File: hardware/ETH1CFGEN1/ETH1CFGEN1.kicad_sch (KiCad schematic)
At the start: 0 parts

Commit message: Development
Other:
- sheet ADC ports: added ADC_CLK, ADC_CONV, ADC_DATA, MEAS_AMPL, MEAS_BUF, MEAS_MOD_DAC, MEAS_OUT, MSEL[0..2]; removed none
- sheet Connector ports: added MAIN_OUTPUT; removed SIGNAL
- sheet DAC ports: added DAC_DIN, DAC_SCLK, DAC_nCLR, DAC_nLDAC, DAC_nSYNC; removed none
- sheet MCU ports: added I2C2_SCL, I2C2_SDA, SPI2_CLK, SPI2_CS, SPI2_MISO, SPI2_MOSI; removed GPIO1, GPIO2, I2C_SCL, I2C_SDA, SPI1_CLK, SPI1_CS, SPI1_MISO, SPI1_MOSI
- sheet Output ports: added MAIN_OUTPUT, MEAS_BUF, MEAS_OUT, OUTPUT_ENABLE, OUTPUT_FAULT, RST_+20DB, RST_-10DB, RST_-20DB, SET_+20DB, SET_-10DB, SET_-20DB, SET_SIN_ARB, SET_SQ_PLS, SINE_ARB, SQ_PLS, V_OFFSET; removed none
- sheet Self test ports: added ADC_I2C_SCL, ADC_I2C_SDA; removed I2C_SCL, I2C_SDA

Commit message: PCB design
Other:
- sheet FPGA ports: added WFDAC[0..13]; removed none
- sheet MCU ports: added none; removed SPI2_CLK, SPI2_CS, SPI2_MISO, SPI2_MOSI

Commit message: PCB design
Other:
- sheet FPGA ports: added MCU_SPI_CLK, MCU_SPI_MISO, MCU_SPI_MOSI, MCU_SPI_NSS; removed none
- sheet MCU ports: added MCU_SPI_CLK, MCU_SPI_MISO, MCU_SPI_MOSI, MCU_SPI_NSS; removed none
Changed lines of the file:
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@@
+    (stroke (width 0) (type default))
+  )
+  (wire (pts (xy 166.37 93.98) (xy 175.895 93.98))
     (stroke (width 0) (type default))
   )
@@
     (stroke (width 0) (type default))
   )
+  (wire (pts (xy 166.37 97.79) (xy 175.895 97.79))
+    (stroke (width 0) (type default))
+  )
   (wire (pts (xy 214.63 121.285) (xy 220.345 121.285))
     (stroke (width 0) (type default))
@@
     (stroke (width 0) (type default))
   )
+  (wire (pts (xy 166.37 99.695) (xy 175.895 99.695))
+    (stroke (width 0) (type default))
+  )
   (wire (pts (xy 214.63 113.665) (xy 220.345 113.665))
+    (stroke (width 0) (type default))
+  )
+  (wire (pts (xy 166.37 95.885) (xy 175.895 95.885))
     (stroke (width 0) (type default))
   )
@@
       (effects (font (size 1.27 1.27)) (justify left))
     )
+    (pin "MCU_SPI_NSS" output (at 175.895 93.98 180)
+      (effects (font (size 1.27 1.27)) (justify left))
+    )
+    (pin "MCU_SPI_MOSI" output (at 175.895 95.885 180)
+      (effects (font (size 1.27 1.27)) (justify left))
+    )
+    (pin "MCU_SPI_MISO" input (at 175.895 97.79 180)
+      (effects (font (size 1.27 1.27)) (justify left))
+    )
+    (pin "MCU_SPI_CLK" output (at 175.895 99.695 180)
+      (effects (font (size 1.27 1.27)) (justify left))
+    )
     (instances
       (project "ETH1CFGEN1"
@@
       (effects (font (size 1.27 1.27)) (justify left))
     )
-    (instances
+    (pin "MCU_SPI_NSS" input (at 166.37 93.98 0)
+      (effects (font (size 1.27 1.27)) (justify right))
+    )
+    (pin "MCU_SPI_MOSI" input (at 166.37 95.885 0)
+      (effects (font (size 1.27 1.27)) (justify right))
+    )
+    (pin "MCU_SPI_MISO" output (at 166.37 97.79 0)
+      (effects (font (size 1.27 1.27)) (justify right))
+    )
+    (pin "MCU_SPI_CLK" input (at 166.37 99.695 0)
+      (effects (font (size 1.27 1.27)) (justify right))
+    )
+    (instances

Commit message: PCB design
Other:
- sheet Output ports: added REL_+20DB, REL_-10DB, REL_-20DB, REL_SQ-SIN; removed RST_+20DB, RST_-10DB, RST_-20DB, SET_+20DB, SET_-10DB, SET_-20DB, SET_SIN_ARB, SET_SQ_PLS
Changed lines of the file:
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@@
       (effects (font (size 1.27 1.27)) (justify right))
     )
-    (pin "SET_-20DB" input (at 175.895 65.405 180)
-      (effects (font (size 1.27 1.27)) (justify left))
-    )
-    (pin "RST_-20DB" input (at 175.895 67.31 180)
-      (effects (font (size 1.27 1.27)) (justify left))
-    )
-    (pin "RST_-10DB" input (at 175.895 62.865 180)
-      (effects (font (size 1.27 1.27)) (justify left))
-    )
-    (pin "V_OFFSET" input (at 175.895 52.705 180)
-      (effects (font (size 1.27 1.27)) (justify left))
-    )
-    (pin "SET_-10DB" input (at 175.895 60.96 180)
-      (effects (font (size 1.27 1.27)) (justify left))
-    )
     (pin "MEAS_BUF" output (at 175.895 79.375 180)
-      (effects (font (size 1.27 1.27)) (justify left))
-    )
-    (pin "SINE_ARB" input (at 175.895 48.895 180)
-      (effects (font (size 1.27 1.27)) (justify left))
-    )
-    (pin "SET_SQ_PLS" input (at 175.895 69.85 180)
-      (effects (font (size 1.27 1.27)) (justify left))
-    )
-    (pin "SET_SIN_ARB" input (at 175.895 71.755 180)
-      (effects (font (size 1.27 1.27)) (justify left))
-    )
-    (pin "SQ_PLS" input (at 175.895 50.8 180)
-      (effects (font (size 1.27 1.27)) (justify left))
-    )
-    (pin "RST_+20DB" input (at 175.895 58.42 180)
-      (effects (font (size 1.27 1.27)) (justify left))
-    )
-    (pin "SET_+20DB" input (at 175.895 56.515 180)
       (effects (font (size 1.27 1.27)) (justify left))
     )
@@
       (effects (font (size 1.27 1.27)) (justify left))
     )
+    (pin "REL_-20DB" input (at 175.895 49.53 180)
+      (effects (font (size 1.27 1.27)) (justify left))
+    )
+    (pin "REL_+20DB" input (at 175.895 51.435 180)
+      (effects (font (size 1.27 1.27)) (justify left))
+    )
+    (pin "V_OFFSET" input (at 175.895 53.34 180)
+      (effects (font (size 1.27 1.27)) (justify left))
+    )
+    (pin "REL_-10DB" input (at 175.895 55.245 180)
+      (effects (font (size 1.27 1.27)) (justify left))
+    )
+    (pin "SQ_PLS" input (at 175.895 57.15 180)
+      (effects (font (size 1.27 1.27)) (justify left))
+    )
+    (pin "SINE_ARB" input (at 175.895 59.055 180)
+      (effects (font (size 1.27 1.27)) (justify left))
+    )
+    (pin "REL_SQ-SIN" input (at 175.895 60.96 180)
+      (effects (font (size 1.27 1.27)) (justify left))
+    )

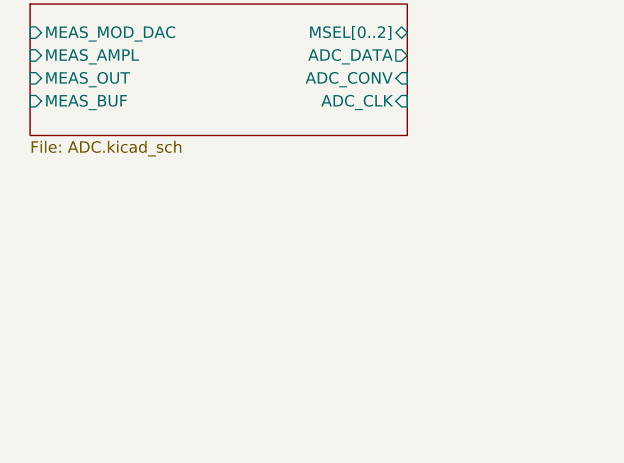
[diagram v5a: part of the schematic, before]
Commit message: Added SDRAM
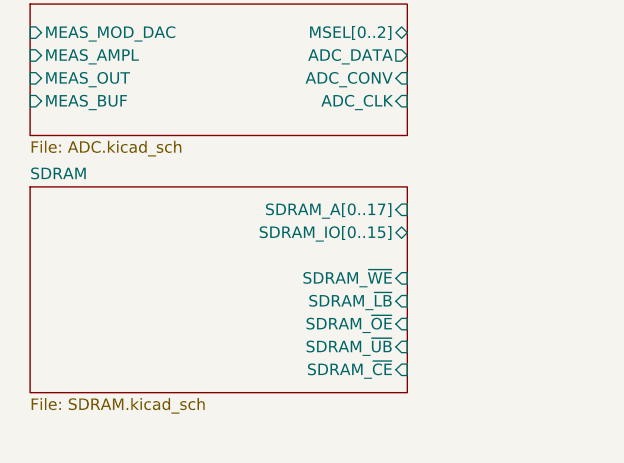
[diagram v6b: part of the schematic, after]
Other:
- added sheet SDRAM (SDRAM.kicad_sch)
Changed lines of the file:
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@@
+    )
+  )
+  (sheet (at 53.975 148.59) (size 41.91 22.86) (fields_autoplaced)
+    (stroke (width 0.1524) (type solid))
+    (fill (color 0 0 0 0.0000))
+    (property "Sheetname" "SDRAM" (at 53.975 147.8784 0)
+      (effects (font (size 1.27 1.27)) (justify left bottom))
+    )
+    (property "Sheetfile" "SDRAM.kicad_sch" (at 53.975 172.0346 0)
+      (effects (font (size 1.27 1.27)) (justify left top))
+    )
+    (pin "SDRAM_A[0..17]" input (at 95.885 151.13 0)
+      (effects (font (size 1.27 1.27)) (justify right))
+    )
+    (pin "SDRAM_IO[0..15]" bidirectional (at 95.885 153.67 0)
+      (effects (font (size 1.27 1.27)) (justify right))
+    )
+    (pin "SDRAM_~{WE}" input (at 95.885 158.75 0)
+      (effects (font (size 1.27 1.27)) (justify right))
+    )
+    (pin "SDRAM_~{LB}" input (at 95.885 161.29 0)
+      (effects (font (size 1.27 1.27)) (justify right))
+    )
+    (pin "SDRAM_~{OE}" input (at 95.885 163.83 0)
+      (effects (font (size 1.27 1.27)) (justify right))
+    )
+    (pin "SDRAM_~{UB}" input (at 95.885 166.37 0)
+      (effects (font (size 1.27 1.27)) (justify right))
+    )
+    (pin "SDRAM_~{CE}" input (at 95.885 168.91 0)
+      (effects (font (size 1.27 1.27)) (justify right))
+    )
+    (instances
+      (project "ETH1CFGEN1"
+        (path "/44bc1157-6d68-4ab3-afc0-b8d9f089cc50" (page "14"))
+      )
     )
   )

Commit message: Schematic and PCB design
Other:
- sheet FPGA ports: added MCU_GPIO1, MCU_GPIO2, SDRAM_A[0..17], SDRAM_IO[0..15], SDRAM_~{CE}, SDRAM_~{LB}, SDRAM_~{OE}, SDRAM_~{UB}, SDRAM_~{WE}; removed none
- sheet MCU ports: added MCU_GPIO1, MCU_GPIO2; removed none
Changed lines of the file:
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@@
     (rev "1.1")
   )
+  (wire (pts (xy 95.885 168.91) (xy 126.365 168.91))
+    (stroke (width 0) (type default))
+  )
+  (wire (pts (xy 121.285 163.83) (xy 121.285 143.51))
+    (stroke (width 0) (type default))
+  )
   (wire (pts (xy 214.63 101.6) (xy 252.095 101.6))
     (stroke (width 0) (type default))
@@
     (stroke (width 0) (type default))
   )
-  (wire (pts (xy 171.45 168.275) (xy 171.45 145.415))
+  (wire (pts (xy 171.45 161.29) (xy 171.45 145.415))
     (stroke (width 0) (type default))
   )
@@
     (stroke (width 0) (type default))
   )
-  (wire (pts (xy 166.37 168.275) (xy 171.45 168.275))
+  (wire (pts (xy 166.37 161.29) (xy 171.45 161.29))
     (stroke (width 0) (type default))
   )
@@
     (stroke (width 0) (type default))
   )
+  (wire (pts (xy 118.745 161.29) (xy 118.745 140.97))
+    (stroke (width 0) (type default))
+  )
+  (bus (pts (xy 95.885 153.67) (xy 113.665 153.67))
+    (stroke (width 0) (type default))
+  )
   (wire (pts (xy 166.37 99.695) (xy 175.895 99.695))
     (stroke (width 0) (type default))
   )
+  (wire (pts (xy 126.365 148.59) (xy 131.445 148.59))
+    (stroke (width 0) (type default))
+  )
+  (bus (pts (xy 113.665 133.35) (xy 131.445 133.35))
+    (stroke (width 0) (type default))
+  )
   (wire (pts (xy 214.63 113.665) (xy 220.345 113.665))
     (stroke (width 0) (type default))
   )
+  (wire (pts (xy 116.205 138.43) (xy 131.445 138.43))
+    (stroke (width 0) (type default))
+  )
   (wire (pts (xy 166.37 95.885) (xy 175.895 95.885))
     (stroke (width 0) (type default))
@@
     (stroke (width 0) (type default))
   )
-  (wire (pts (xy 173.355 170.18) (xy 173.355 147.32))
+  (bus (pts (xy 95.885 151.13) (xy 111.125 151.13))
+    (stroke (width 0) (type default))
+  )
+  (wire (pts (xy 173.355 163.195) (xy 173.355 147.32))
     (stroke (width 0) (type default))
   )
@@
     (stroke (width 0) (type default))
   )
+  (wire (pts (xy 95.885 166.37) (xy 123.825 166.37))
+    (stroke (width 0) (type default))
+  )
   (wire (pts (xy 247.65 113.665) (xy 252.095 113.665))
     (stroke (width 0) (type default))
@@
     (stroke (width 0) (type default))
   )
+  (wire (pts (xy 166.37 101.6) (xy 175.895 101.6))
+    (stroke (width 0) (type default))
+  )
   (bus (pts (xy 131.445 93.98) (xy 125.73 93.98))
     (stroke (width 0) (type default))
   )
+  (wire (pts (xy 118.745 140.97) (xy 131.445 140.97))
+    (stroke (width 0) (type default))
+  )
+  (wire (pts (xy 116.205 158.75) (xy 116.205 138.43))
+    (stroke (width 0) (type default))
+  )
+  (wire (pts (xy 95.885 158.75) (xy 116.205 158.75))
+    (stroke (width 0) (type default))
+  )
+  (wire (pts (xy 95.885 161.29) (xy 118.745 161.29))
+    (stroke (width 0) (type default))
+  )
   (wire (pts (xy 214.63 123.19) (xy 220.345 123.19))
     (stroke (width 0) (type default))
   )
+  (wire (pts (xy 95.885 163.83) (xy 121.285 163.83))
+    (stroke (width 0) (type default))
+  )
+  (wire (pts (xy 126.365 168.91) (xy 126.365 148.59))
+    (stroke (width 0) (type default))
+  )
   (wire (pts (xy 214.63 145.415) (xy 220.345 145.415))
     (stroke (width 0) (type default))
   )
+  (wire (pts (xy 121.285 143.51) (xy 131.445 143.51))
+    (stroke (width 0) (type default))
+  )
+  (wire (pts (xy 123.825 146.05) (xy 131.445 146.05))
+    (stroke (width 0) (type default))
+  )
+  (wire (pts (xy 166.37 103.505) (xy 175.895 103.505))
+    (stroke (width 0) (type default))
+  )
   (wire (pts (xy 214.63 99.695) (xy 252.095 99.695))
     (stroke (width 0) (type default))
@@
     (stroke (width 0) (type default))
   )
+  (bus (pts (xy 111.125 151.13) (xy 111.125 130.81))
+    (stroke (width 0) (type default))
+  )
+  (bus (pts (xy 111.125 130.81) (xy 131.445 130.81))
+    (stroke (width 0) (type default))
+  )
   (wire (pts (xy 214.63 97.79) (xy 252.095 97.79))
     (stroke (width 0) (type default))
@@
     (stroke (width 0) (type default))
   )
-  (wire (pts (xy 166.37 170.18) (xy 173.355 170.18))
+  (wire (pts (xy 166.37 163.195) (xy 173.355 163.195))
+    (stroke (width 0) (type default))
+  )
+  (bus (pts (xy 113.665 153.67) (xy 113.665 133.35))
     (stroke (width 0) (type default))
   )
@@
     (stroke (width 0) (type default))
   )
+  (wire (pts (xy 123.825 166.37) (xy 123.825 146.05))
+    (stroke (width 0) (type default))
+  )
   (wire (pts (xy 214.63 127) (xy 220.345 127))
     (stroke (width 0) (type default))
@@
       (effects (font (size 1.27 1.27)) (justify left))
     )
+    (pin "MCU_GPIO1" bidirectional (at 175.895 101.6 180)
+      (effects (font (size 1.27 1.27)) (justify left))
+    )
+    (pin "MCU_GPIO2" bidirectional (at 175.895 103.505 180)
+      (effects (font (size 1.27 1.27)) (justify left))
+    )
     (instances
       (project "ETH1CFGEN1"
@@
       (effects (font (size 1.27 1.27)) (justify right))
     )
+    (pin "SDRAM_A[0..17]" input (at 131.445 130.81 180)
+      (effects (font (size 1.27 1.27)) (justify left))
+    )
+    (pin "SDRAM_IO[0..15]" bidirectional (at 131.445 133.35 180)
+      (effects (font (size 1.27 1.27)) (justify left))
+    )
+    (pin "SDRAM_~{UB}" output (at 131.445 146.05 180)
+      (effects (font (size 1.27 1.27)) (justify left))
+    )
+    (pin "SDRAM_~{OE}" output (at 131.445 143.51 180)
+      (effects (font (size 1.27 1.27)) (justify left))
+    )
+    (pin "SDRAM_~{WE}" output (at 131.445 138.43 180)
+      (effects (font (size 1.27 1.27)) (justify left))
+    )
+    (pin "SDRAM_~{LB}" output (at 131.445 140.97 180)
+      (effects (font (size 1.27 1.27)) (justify left))
+    )
+    (pin "SDRAM_~{CE}" output (at 131.445 148.59 180)
+      (effects (font (size 1.27 1.27)) (justify left))
+    )
+    (pin "MCU_GPIO2" bidirectional (at 166.37 103.505 0)
+      (effects (font (size 1.27 1.27)) (justify right))
+    )
+    (pin "MCU_GPIO1" bidirectional (at 166.37 101.6 0)
+      (effects (font (size 1.27 1.27)) (justify right))
+    )
     (instances
       (project "ETH1CFGEN1"
@@
     )
   )
-  (sheet (at 131.445 165.1) (size 34.925 9.525) (fields_autoplaced)
-    (stroke (width 0.1524) (type solid))
-    (fill (color 0 0 0 0.0000))
-    (property "Sheetname" "Self test" (at 131.445 164.3884 0)
-      (effects (font (size 1.27 1.27)) (justify left bottom))
-    )
-    (property "Sheetfile" "SelftTest.kicad_sch" (at 131.445 175.2096 0)
-      (effects (font (size 1.27 1.27)) (justify left top))
-    )
-    (pin "ADC_I2C_SCL" bidirectional (at 166.37 168.275 0)
-      (effects (font (size 1.27 1.27)) (justify right))
-    )
-    (pin "ADC_I2C_SDA" bidirectional (at 166.37 170.18 0)
-      (effects (font (size 1.27 1.27)) (justify right))
-    )
+  (sheet (at 131.445 158.115) (size 34.925 9.525) (fields_autoplaced)
+    (stroke (width 0.1524) (type solid))
+    (fill (color 0 0 0 0.0000))
+    (property "Sheetname" "Self test" (at 131.445 157.4034 0)
+      (effects (font (size 1.27 1.27)) (justify left bottom))
+    )
+    (property "Sheetfile" "SelftTest.kicad_sch" (at 131.445 168.2246 0)
+      (effects (font (size 1.27 1.27)) (justify left top))
+    )
+    (pin "ADC_I2C_SCL" bidirectional (at 166.37 161.29 0)
+      (effects (font (size 1.27 1.27)) (justify right))
+    )
+    (pin "ADC_I2C_SDA" bidirectional (at 166.37 163.195 0)
+      (effects (font (size 1.27 1.27)) (justify right))
+    )

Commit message: FPGA code
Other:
- sheet FPGA ports: added ADC_CLK, ADC_CONV, ADC_DATA, DAC_DIN, DAC_SCLK, DAC_nCLR, DAC_nLDAC, DAC_nSYNC, MSEL[0..2], SET_SIN-ARB_FLTR1, SET_SIN-ARB_FLTR2, SQ_AMPL_CLK, SQ_AMPL_DATA, SQ_AMPL_LE, SQ_COMP_EN, WFD_FPGA_50MHZ; removed none
- sheet WaveformDAC ports: added SET_SIN-ARB_FLTR1, SET_SIN-ARB_FLTR2; removed SET_ARB_FLTR1, SET_ARB_FLTR2, SET_SIN_FLTR1, SET_SIN_FLTR2
